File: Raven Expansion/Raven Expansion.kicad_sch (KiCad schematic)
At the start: 3 parts, among them J1 Conn_01x06_Pin, J2 Screw_Terminal_01x06, J3 Screw_Terminal_01x06

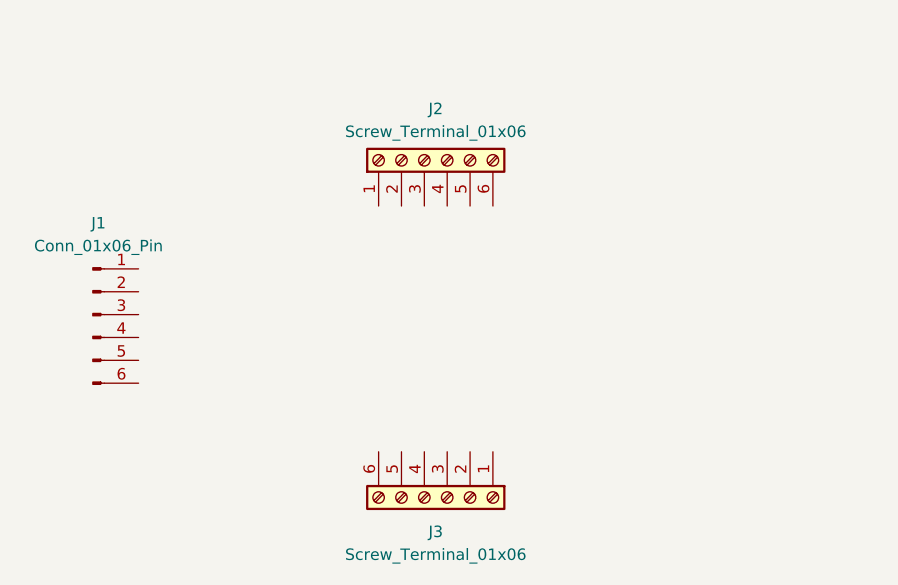
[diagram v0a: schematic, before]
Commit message: Raven expansion
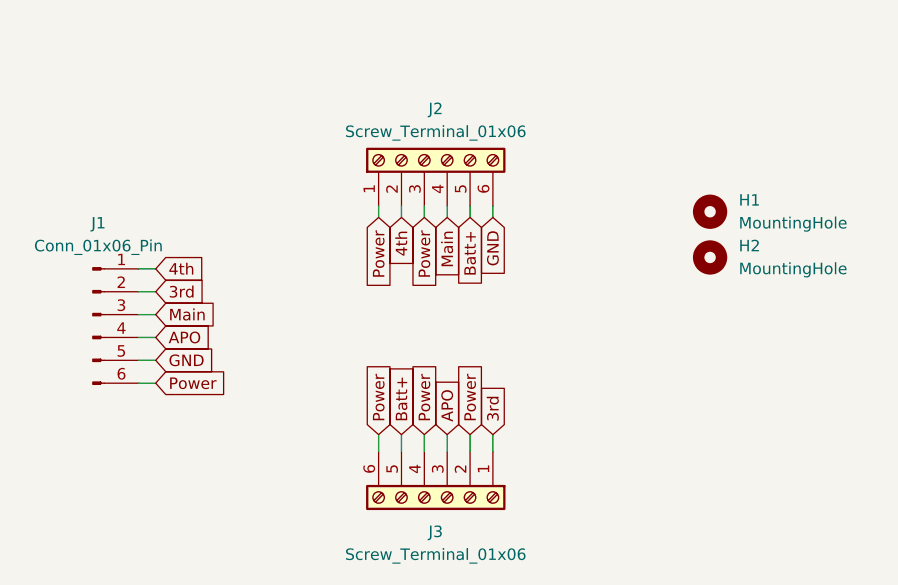
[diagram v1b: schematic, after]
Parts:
- added H1, H2: MountingHole, MountingHole:MountingHole_3.2mm_M3, symbol Mechanical:MountingHole
- J2, J3: footprint (none) -> TerminalBlock_Phoenix:TerminalBlock_Phoenix_PT-1,5-6-3.5-H_1x06_P3.50mm_Horizontal
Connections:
- net 4th: now reaches J1.1 (Pin_1)
- net 4th: now also J2.2 (Pin_2)
- net 3rd: now reaches J1.2 (Pin_2)
- net 3rd: now also J3.1 (Pin_1)
- net Main: now reaches J1.3 (Pin_3)
- net Main: now also J2.4 (Pin_4)
- net APO: now reaches J1.4 (Pin_4)
- net APO: now also J3.3 (Pin_3)
- net GND: now reaches J1.5 (Pin_5)
- net GND: now also J2.6 (Pin_6)
- net Power: now reaches J1.6 (Pin_6)
- net Power: now also J2.1 (Pin_1), J2.3 (Pin_3), J3.2 (Pin_2), J3.4 (Pin_4), J3.6 (Pin_6)
- net Batt+: now reaches J3.5 (Pin_5)
- net Batt+: now also J2.5 (Pin_5)
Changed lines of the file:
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@@
 (kicad_sch (version 20230121) (generator eeschema)
   (paper "A4")
+  (wire (pts (xy 97.79 74.93) (xy 95.885 74.93))
+    (stroke (width 0) (type default))
+  )
+  (wire (pts (xy 122.555 59.055) (xy 122.555 57.785))
+    (stroke (width 0) (type default))
+  )
+  (wire (pts (xy 135.255 59.055) (xy 135.255 57.785))
+    (stroke (width 0) (type default))
+  )
+  (wire (pts (xy 135.255 83.185) (xy 135.255 85.09))
+    (stroke (width 0) (type default))
+  )
+  (wire (pts (xy 97.79 67.31) (xy 95.885 67.31))
+    (stroke (width 0) (type default))
+  )
+  (wire (pts (xy 97.79 69.85) (xy 95.885 69.85))
+    (stroke (width 0) (type default))
+  )
+  (wire (pts (xy 125.095 59.055) (xy 125.095 57.785))
+    (stroke (width 0) (type default))
+  )
+  (wire (pts (xy 122.555 83.185) (xy 122.555 85.09))
+    (stroke (width 0) (type default))
+  )
+  (wire (pts (xy 97.79 72.39) (xy 95.885 72.39))
+    (stroke (width 0) (type default))
+  )
+  (wire (pts (xy 130.175 83.185) (xy 130.175 85.09))
+    (stroke (width 0) (type default))
+  )
+  (wire (pts (xy 132.715 83.185) (xy 132.715 85.09))
+    (stroke (width 0) (type default))
+  )
+  (wire (pts (xy 132.715 59.055) (xy 132.715 57.785))
+    (stroke (width 0) (type default))
+  )
+  (wire (pts (xy 97.79 64.77) (xy 95.885 64.77))
+    (stroke (width 0) (type default))
+  )
+  (wire (pts (xy 97.79 77.47) (xy 95.885 77.47))
+    (stroke (width 0) (type default))
+  )
+  (wire (pts (xy 127.635 83.185) (xy 127.635 85.09))
+    (stroke (width 0) (type default))
+  )
+  (wire (pts (xy 127.635 59.055) (xy 127.635 57.785))
+    (stroke (width 0) (type default))
+  )
+  (wire (pts (xy 130.175 59.055) (xy 130.175 57.785))
+    (stroke (width 0) (type default))
+  )
+  (wire (pts (xy 125.095 83.185) (xy 125.095 85.09))
+    (stroke (width 0) (type default))
+  )
+  (global_label "Batt+" (shape input) (at 132.715 59.055 270) (fields_autoplaced)
+    (effects (font (size 1.27 1.27)) (justify right))
+    (property "Intersheetrefs" "${INTERSHEET_REFS}" (at 132.715 67.483 90)
+      (effects (font (size 1.27 1.27)) (justify left) hide)
+    )
+  )
+  (global_label "4th" (shape input) (at 125.095 59.055 270) (fields_autoplaced)
+    (effects (font (size 1.27 1.27)) (justify right))
+    (property "Intersheetrefs" "${INTERSHEET_REFS}" (at 125.095 65.1244 90)
+      (effects (font (size 1.27 1.27)) (justify left) hide)
+    )
+  )
+  (global_label "APO" (shape input) (at 130.175 83.185 90) (fields_autoplaced)
+    (effects (font (size 1.27 1.27)) (justify left))
+    (property "Intersheetrefs" "${INTERSHEET_REFS}" (at 130.175 76.5107 90)
+      (effects (font (size 1.27 1.27)) (justify left) hide)
+    )
+  )
+  (global_label "3rd" (shape input) (at 135.255 83.185 90) (fields_autoplaced)
+    (effects (font (size 1.27 1.27)) (justify left))
+    (property "Intersheetrefs" "${INTERSHEET_REFS}" (at 135.255 77.0551 90)
+      (effects (font (size 1.27 1.27)) (justify left) hide)
+    )
+  )
+  (global_label "APO" (shape input) (at 97.79 72.39 0) (fields_autoplaced)
+    (effects (font (size 1.27 1.27)) (justify left))
+    (property "Intersheetrefs" "${INTERSHEET_REFS}" (at 104.4643 72.39 0)
+      (effects (font (size 1.27 1.27)) (justify left) hide)
+    )
+  )
+  (global_label "Power" (shape input) (at 127.635 83.185 90) (fields_autoplaced)
+    (effects (font (size 1.27 1.27)) (justify left))
+    (property "Intersheetrefs" "${INTERSHEET_REFS}" (at 127.635 74.5755 90)
+      (effects (font (size 1.27 1.27)) (justify right) hide)
+    )
+  )
+  (global_label "Batt+" (shape input) (at 125.095 83.185 90) (fields_autoplaced)
+    (effects (font (size 1.27 1.27)) (justify left))
+    (property "Intersheetrefs" "${INTERSHEET_REFS}" (at 125.095 74.757 90)
+      (effects (font (size 1.27 1.27)) (justify left) hide)
+    )
+  )
+  (global_label "GND" (shape input) (at 135.255 59.055 270) (fields_autoplaced)
+    (effects (font (size 1.27 1.27)) (justify right))
+    (property "Intersheetrefs" "${INTERSHEET_REFS}" (at 135.255 65.9107 90)
+      (effects (font (size 1.27 1.27)) (justify left) hide)
+    )
+  )
+  (global_label "Power" (shape input) (at 97.79 77.47 0) (fields_autoplaced)
+    (effects (font (size 1.27 1.27)) (justify left))
+    (property "Intersheetrefs" "${INTERSHEET_REFS}" (at 106.3995 77.47 0)
+      (effects (font (size 1.27 1.27)) (justify left) hide)
+    )
+  )
+  (global_label "Main" (shape input) (at 97.79 69.85 0) (fields_autoplaced)
+    (effects (font (size 1.27 1.27)) (justify left))
+    (property "Intersheetrefs" "${INTERSHEET_REFS}" (at 105.1294 69.85 0)
+      (effects (font (size 1.27 1.27)) (justify left) hide)
+    )
+  )
+  (global_label "Power" (shape input) (at 132.715 83.185 90) (fields_autoplaced)
+    (effects (font (size 1.27 1.27)) (justify left))
+    (property "Intersheetrefs" "${INTERSHEET_REFS}" (at 132.715 74.5755 90)
+      (effects (font (size 1.27 1.27)) (justify right) hide)
+    )
+  )
+  (global_label "Main" (shape input) (at 130.175 59.055 270) (fields_autoplaced)
+    (effects (font (size 1.27 1.27)) (justify right))
+    (property "Intersheetrefs" "${INTERSHEET_REFS}" (at 130.175 66.3944 90)
+      (effects (font (size 1.27 1.27)) (justify left) hide)
+    )
+  )
+  (global_label "3rd" (shape input) (at 97.79 67.31 0) (fields_autoplaced)
+    (effects (font (size 1.27 1.27)) (justify left))
+    (property "Intersheetrefs" "${INTERSHEET_REFS}" (at 103.9199 67.31 0)
+      (effects (font (size 1.27 1.27)) (justify left) hide)
+    )
+  )
+  (global_label "4th" (shape input) (at 97.79 64.77 0) (fields_autoplaced)
+    (effects (font (size 1.27 1.27)) (justify left))
+    (property "Intersheetrefs" "${INTERSHEET_REFS}" (at 103.8594 64.77 0)
+      (effects (font (size 1.27 1.27)) (justify left) hide)
+    )
+  )
+  (global_label "GND" (shape input) (at 97.79 74.93 0) (fields_autoplaced)
+    (effects (font (size 1.27 1.27)) (justify left))
+    (property "Intersheetrefs" "${INTERSHEET_REFS}" (at 104.6457 74.93 0)
+      (effects (font (size 1.27 1.27)) (justify left) hide)
+    )
+  )
+  (global_label "Power" (shape input) (at 127.635 59.055 270) (fields_autoplaced)
+    (effects (font (size 1.27 1.27)) (justify right))
+    (property "Intersheetrefs" "${INTERSHEET_REFS}" (at 127.635 67.6645 90)
+      (effects (font (size 1.27 1.27)) (justify left) hide)
+    )
+  )
+  (global_label "Power" (shape input) (at 122.555 83.185 90) (fields_autoplaced)
+    (effects (font (size 1.27 1.27)) (justify left))
+    (property "Intersheetrefs" "${INTERSHEET_REFS}" (at 122.555 74.5755 90)
+      (effects (font (size 1.27 1.27)) (justify left) hide)
+    )
+  )
+  (global_label "Power" (shape input) (at 122.555 59.055 270) (fields_autoplaced)
+    (effects (font (size 1.27 1.27)) (justify right))
+    (property "Intersheetrefs" "${INTERSHEET_REFS}" (at 122.555 67.6645 90)
+      (effects (font (size 1.27 1.27)) (justify left) hide)
+    )
+  )
   (symbol (lib_id "Connector:Conn_01x06_Pin") (at 90.805 69.85 0) (unit 1)
     (in_bom yes) (on_board yes) (dnp no) (fields_autoplaced)
@@
     )
   )
+  (symbol (lib_id "Mechanical:MountingHole") (at 159.385 63.5 0) (unit 1)
+    (in_bom yes) (on_board yes) (dnp no) (fields_autoplaced)
+    (property "Reference" "H2" (at 162.56 62.23 0)
+      (effects (font (size 1.27 1.27)) (justify left))
+    )
+    (property "Value" "MountingHole" (at 162.56 64.77 0)
+      (effects (font (size 1.27 1.27)) (justify left))
+    )
+    (property "Footprint" "MountingHole:MountingHole_3.2mm_M3" (at 159.385 63.5 0)
+      (effects (font (size 1.27 1.27)) hide)
+    )
+    (property "Datasheet" "~" (at 159.385 63.5 0)
+      (effects (font (size 1.27 1.27)) hide)
+    )
+    (instances
+      (project "Raven Expansion"
+        (path "/e5d6feef-0371-42fa-a824-66233becfb87"
+          (reference "H2") (unit 1)
+        )
+      )
+    )
+  )
   (symbol (lib_id "Connector:Screw_Terminal_01x06") (at 130.175 90.17 270) (unit 1)
     (in_bom yes) (on_board yes) (dnp no) (fields_autoplaced)
@@
       (effects (font (size 1.27 1.27)))
     )
-    (property "Footprint" "" (at 130.175 90.17 0)
+    (property "Footprint" "TerminalBlock_Phoenix:TerminalBlock_Phoenix_PT-1,5-6-3.5-H_1x06_P3.50mm_Horizontal" (at 130.175 90.17 0)
       (effects (font (size 1.27 1.27)) hide)
     )
@@
       (effects (font (size 1.27 1.27)))
     )
-    (property "Footprint" "" (at 127.635 52.705 0)
+    (property "Footprint" "TerminalBlock_Phoenix:TerminalBlock_Phoenix_PT-1,5-6-3.5-H_1x06_P3.50mm_Horizontal" (at 127.635 52.705 0)
       (effects (font (size 1.27 1.27)) hide)
     )
@@
         )
       )
+    )
+  )
+  (symbol (lib_id "Mechanical:MountingHole") (at 159.385 58.42 0) (unit 1)
+    (in_bom yes) (on_board yes) (dnp no) (fields_autoplaced)
+    (property "Reference" "H1" (at 162.56 57.15 0)
+      (effects (font (size 1.27 1.27)) (justify left))
+    )
+    (property "Value" "MountingHole" (at 162.56 59.69 0)
+      (effects (font (size 1.27 1.27)) (justify left))
+    )
+    (property "Footprint" "MountingHole:MountingHole_3.2mm_M3" (at 159.385 58.42 0)
+      (effects (font (size 1.27 1.27)) hide)
+    )
+    (property "Datasheet" "~" (at 159.385 58.42 0)
+      (effects (font (size 1.27 1.27)) hide)
+    )
+    (instances
+      (project "Raven Expansion"
+        (path "/e5d6feef-0371-42fa-a824-66233becfb87"
+          (reference "H1") (unit 1)
+        )
+      )

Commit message: Ahhhhh
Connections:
- net 3rd: now also J3.6 (Pin_6); no longer J3.1 (Pin_1)
- net APO: now also J3.4 (Pin_4); no longer J3.3 (Pin_3)
- net Batt+: now also J3.2 (Pin_2); no longer J3.5 (Pin_5)
- net Power: now also J3.1 (Pin_1), J3.3 (Pin_3), J3.5 (Pin_5); no longer J3.2 (Pin_2), J3.4 (Pin_4), J3.6 (Pin_6)
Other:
- moved on the sheet: J1, J2, J3
